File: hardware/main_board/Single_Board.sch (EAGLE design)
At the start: 38 parts, among them J1 5520425-3, J2 U.FL, J3 AVR_SPI_PROG_3X2NS, Q1 200mA/40V, Q2 220mA/50V/3.5Ω, U2 MCP1703T-3302E/CB, U3 W25X40CLSNIG, U5 ATMEGA328PB-AU, X2 B2B-PH-K-S, X3 B2B-XH-2, Y1 8MHz

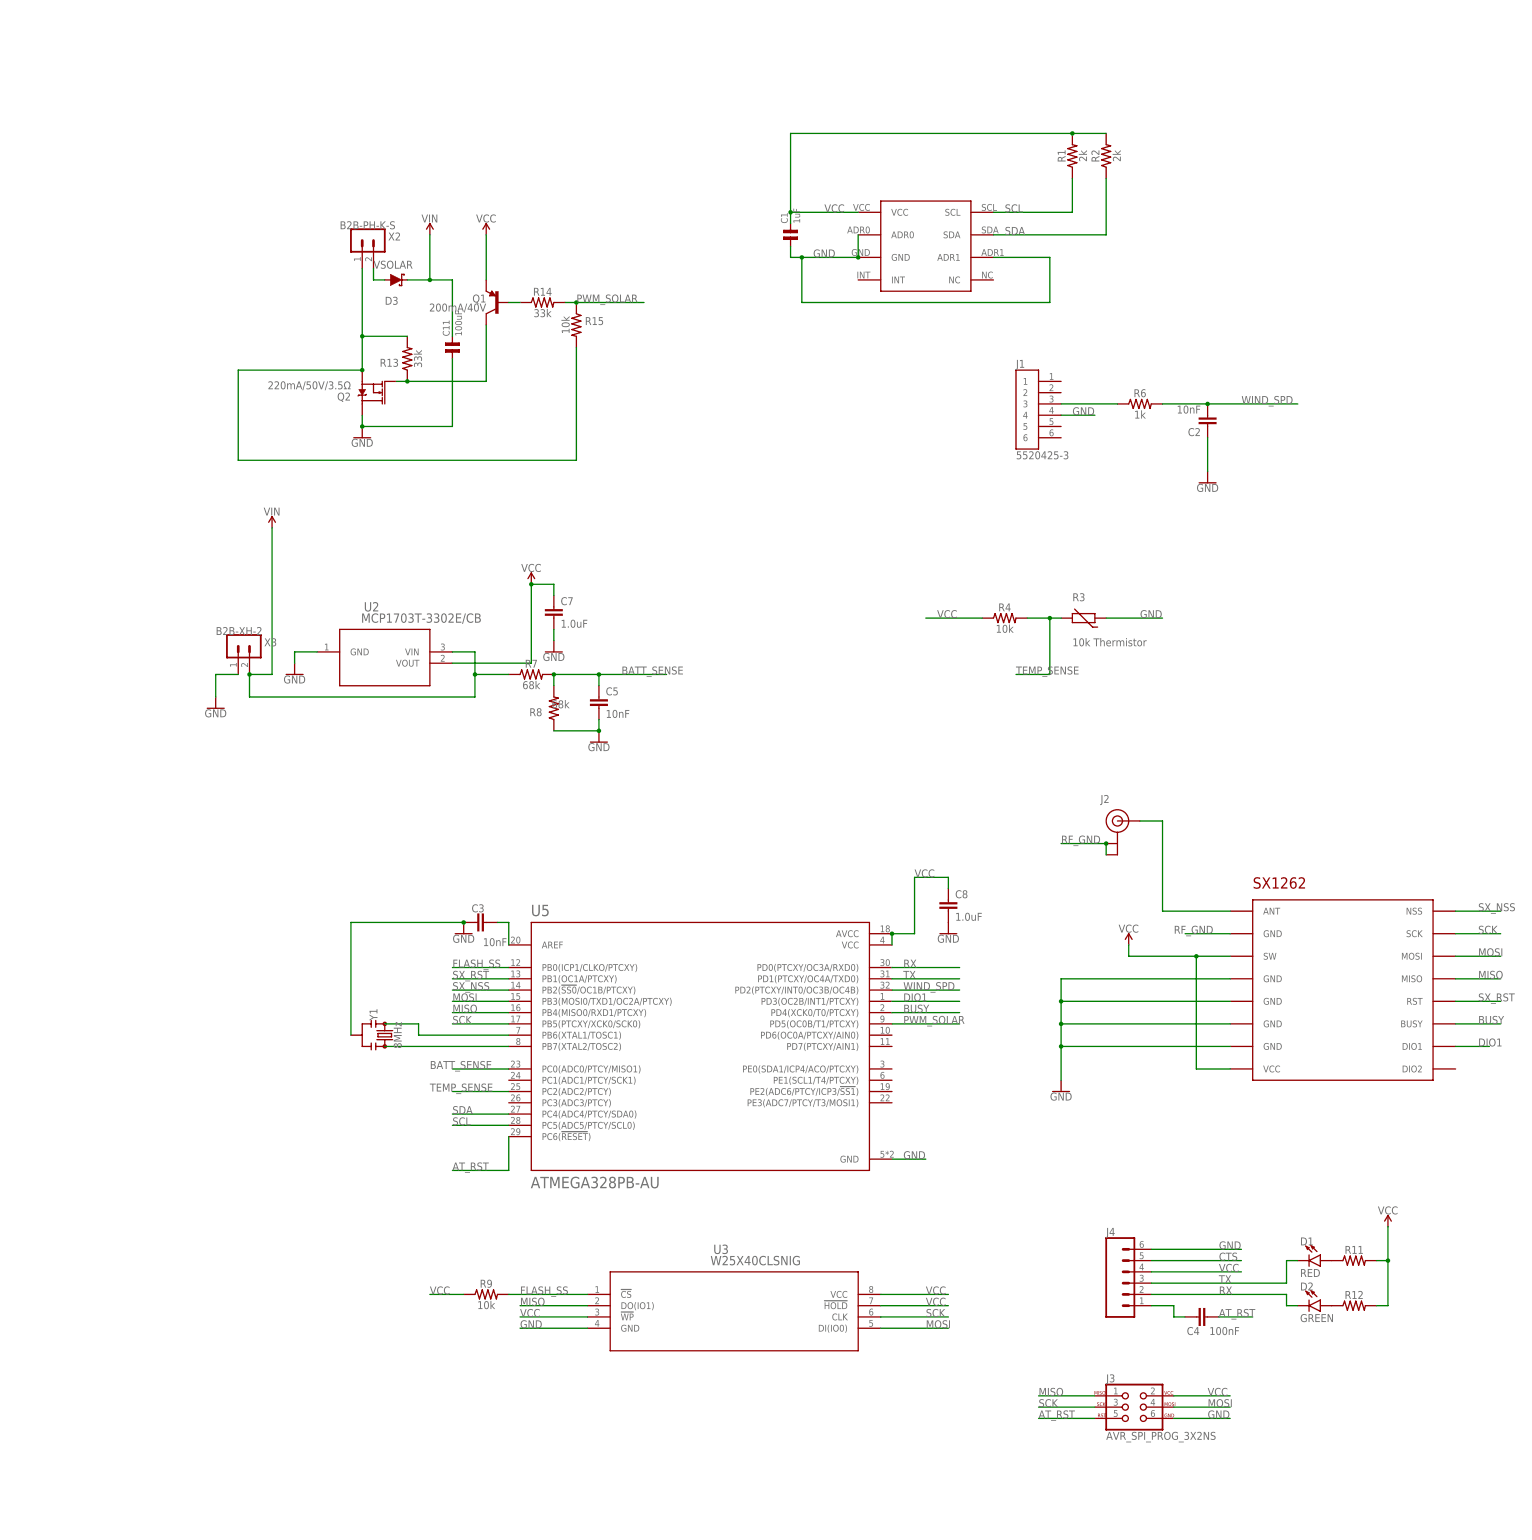
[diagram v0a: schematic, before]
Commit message: Hardware work. Added elevation to station meta data
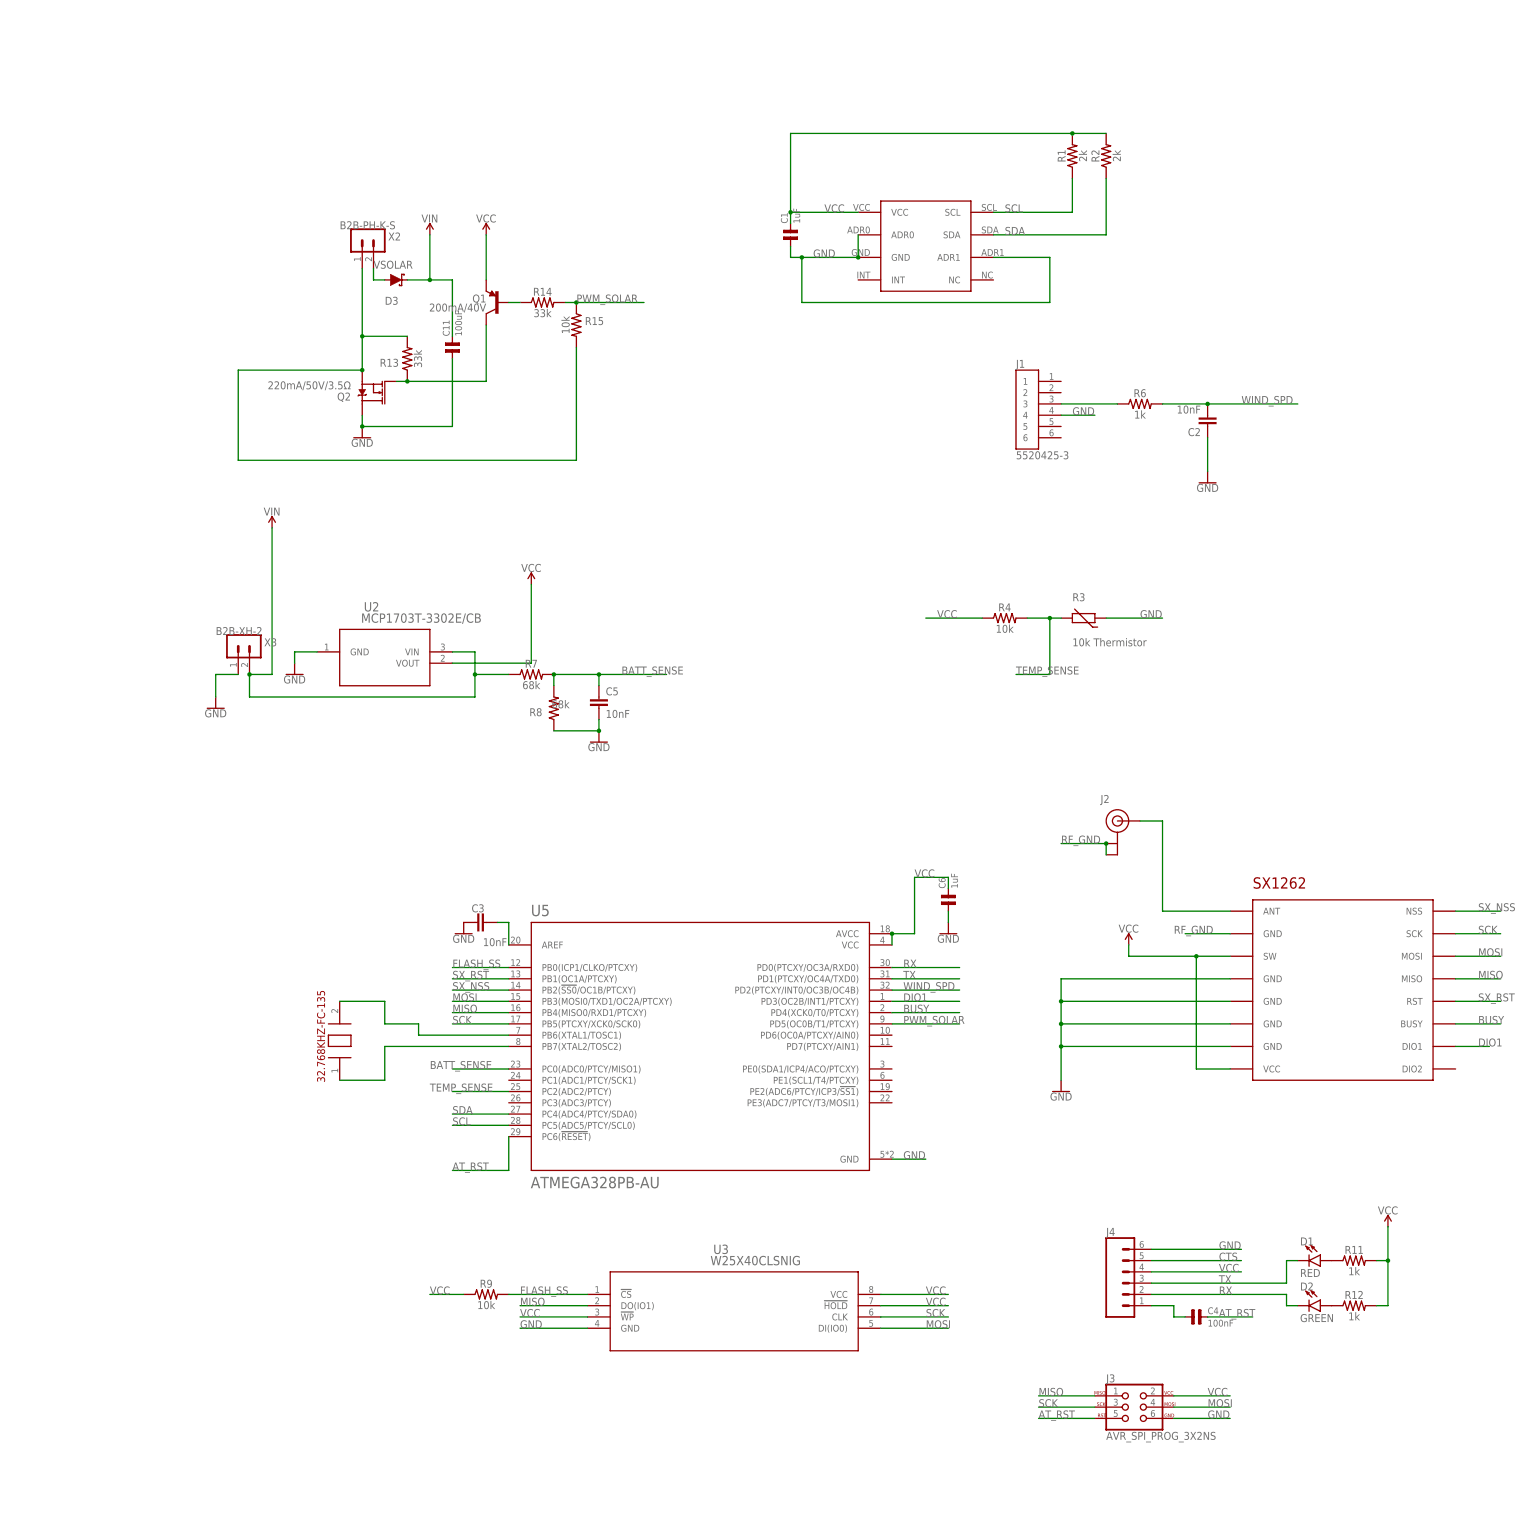
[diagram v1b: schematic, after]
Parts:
- removed C7: 1.0uF, SparkFun-Capacitors:1.0UF-0603-16V-10%
- removed C8: 1.0uF, SparkFun-Capacitors:1.0UF-0805-25V-10%
- removed Y1: 8MHz, SparkFun-Clocks:RESONATOR-8MHZSMD_3.2X1.3
- added C6: 1uF, capsmd:C0805
- added X1: 32.768KHZ-FC-135, main_board:32.768KHZ-FC-135
- C4: device SparkFun-Capacitors:10NF-0603-50V-10% -> main_board:C0805
- R11, R12: value (none) -> 1k
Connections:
- net AT_RST: now also C4.2; no longer C4.1
- net GND: now also C6.1; no longer C7.2, C8.2, Y1.2
- net N$11: now also C4.1; no longer C4.2
- net N$7: now also X1.2.XIN; no longer Y1.1
- net N$8: now also X1.1.XIN; no longer Y1.3
- net VCC: now also C6.2; no longer C7.1, C8.1

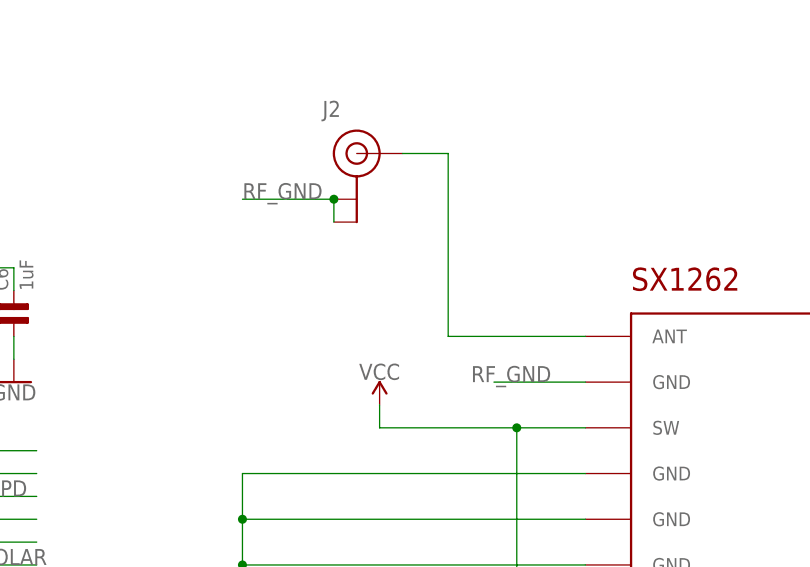
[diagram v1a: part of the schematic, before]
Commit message: Reworked board to put more components on bottom side (=less soldering)
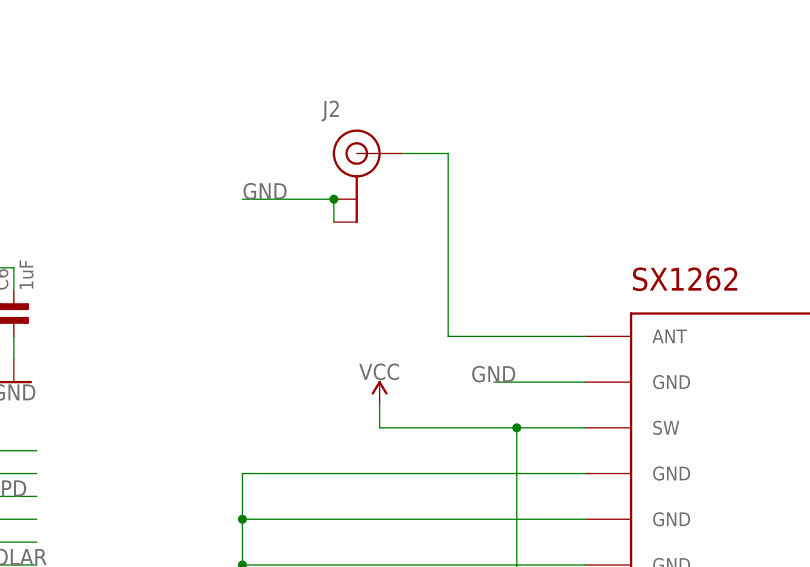
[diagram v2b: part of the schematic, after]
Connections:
- removed net RF_GND: J2.GND@0, J2.GND@1, U$2.GND@1
- net GND: now also J2.GND@0, J2.GND@1, U$2.GND@1
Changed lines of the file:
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@@
 <wire x1="63.5" y1="-93.98" x2="63.5" y2="-96.52" width="0.1524" layer="91"/>
+</segment>
+<segment>
+<wire x1="116.84" y1="-99.06" x2="127" y2="-99.06" width="0.1524" layer="91"/>
+<label x="114.3" y="-99.06" size="1.778" layer="95"/>
+<pinref part="U$2" gate="G$1" pin="GND@1"/>
+</segment>
+<segment>
+<pinref part="J2" gate="G$1" pin="GND@0"/>
+<pinref part="J2" gate="G$1" pin="GND@1"/>
+<wire x1="99.06" y1="-78.74" x2="99.06" y2="-81.28" width="0.1524" layer="91"/>
+<wire x1="99.06" y1="-78.74" x2="88.9" y2="-78.74" width="0.1524" layer="91"/>
+<junction x="99.06" y="-78.74"/>
+<label x="88.9" y="-78.74" size="1.778" layer="95"/>
 </segment>
 </net>
@@
 </segment>
 </net>
-<net name="RF_GND" class="0">
-<segment>
-<wire x1="116.84" y1="-99.06" x2="127" y2="-99.06" width="0.1524" layer="91"/>
-<label x="114.3" y="-99.06" size="1.778" layer="95"/>
-<pinref part="U$2" gate="G$1" pin="GND@1"/>
-</segment>
-<segment>
-<pinref part="J2" gate="G$1" pin="GND@0"/>
-<pinref part="J2" gate="G$1" pin="GND@1"/>
-<wire x1="99.06" y1="-78.74" x2="99.06" y2="-81.28" width="0.1524" layer="91"/>
-<wire x1="99.06" y1="-78.74" x2="88.9" y2="-78.74" width="0.1524" layer="91"/>
-<junction x="99.06" y="-78.74"/>
-<label x="88.9" y="-78.74" size="1.778" layer="95"/>
-</segment>
-</net>
